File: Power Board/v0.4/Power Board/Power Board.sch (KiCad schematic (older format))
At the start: 26 parts, among them J1 Battery In, J2 JST B2PS-VH, J3 JST B2PS-VH, J4 JST B2PS-VH, J5 JST B2PS-VH, J6 JST B2PS-VH, J7 JST B2PS-VH, J8 Molex 70553-0006, SW1 SW_Push

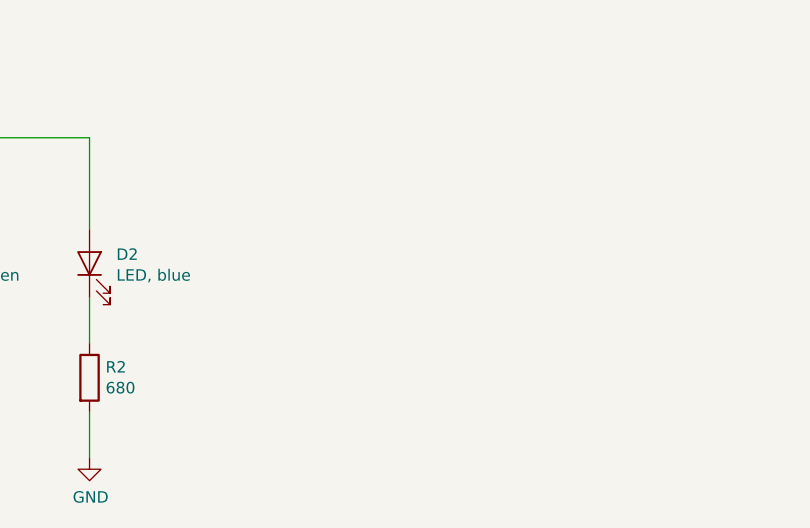
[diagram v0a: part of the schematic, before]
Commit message: Update panel power with Cin, Cout.
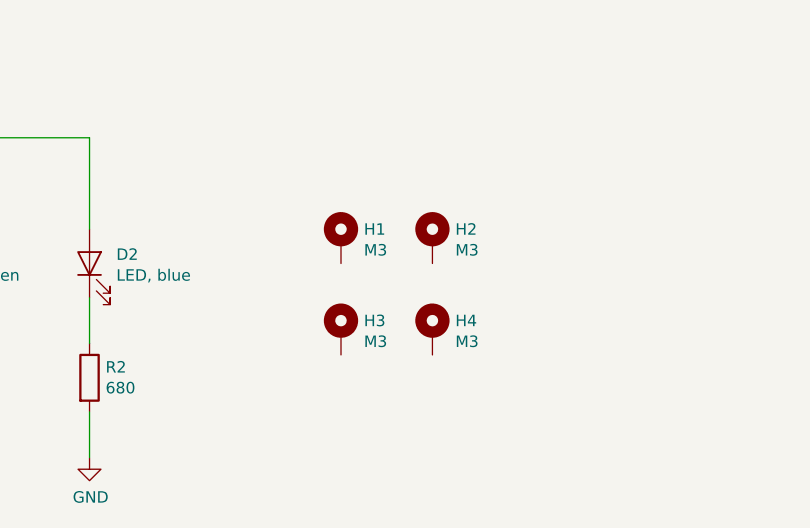
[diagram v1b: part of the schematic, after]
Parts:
- added H1, H2, H3, H4: M3, MountingHole:MountingHole_3.2mm_M3_Pad_Via, symbol Mechanical:MountingHole_Pad
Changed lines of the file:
@@
+	1    0    0    -1
+$EndComp
+$Comp
+L Mechanical:MountingHole_Pad H1
+U 1 1 5CADB5EA
+P 3900 6400
+F 0 "H1" H 4000 6449 50  0000 L CNN
+F 1 "M3" H 4000 6358 50  0000 L CNN
+F 2 "MountingHole:MountingHole_3.2mm_M3_Pad_Via" H 3900 6400 50  0001 C CNN
+F 3 "~" H 3900 6400 50  0001 C CNN
+F 4 "-" H 0   0   50  0001 C CNN "Digikey No."
+F 5 "-" H 0   0   50  0001 C CNN "Manufacturer"
+F 6 "-" H 0   0   50  0001 C CNN "Part No."
+	1    3900 6400
+	1    0    0    -1
+$EndComp
+$Comp
+L Mechanical:MountingHole_Pad H2
+U 1 1 5CADBAB3
+P 4300 6400
+F 0 "H2" H 4400 6449 50  0000 L CNN
+F 1 "M3" H 4400 6358 50  0000 L CNN
+F 2 "MountingHole:MountingHole_3.2mm_M3_Pad_Via" H 4300 6400 50  0001 C CNN
+F 3 "~" H 4300 6400 50  0001 C CNN
+F 4 "-" H 0   0   50  0001 C CNN "Digikey No."
+F 5 "-" H 0   0   50  0001 C CNN "Manufacturer"
+F 6 "-" H 0   0   50  0001 C CNN "Part No."
+	1    4300 6400
+	1    0    0    -1
+$EndComp
+$Comp
+L Mechanical:MountingHole_Pad H4
+U 1 1 5CADBCBF
+P 4300 6800
+F 0 "H4" H 4400 6849 50  0000 L CNN
+F 1 "M3" H 4400 6758 50  0000 L CNN
+F 2 "MountingHole:MountingHole_3.2mm_M3_Pad_Via" H 4300 6800 50  0001 C CNN
+F 3 "~" H 4300 6800 50  0001 C CNN
+F 4 "-" H 0   0   50  0001 C CNN "Digikey No."
+F 5 "-" H 0   0   50  0001 C CNN "Manufacturer"
+F 6 "-" H 0   0   50  0001 C CNN "Part No."
+	1    4300 6800
+	1    0    0    -1
+$EndComp
+$Comp
+L Mechanical:MountingHole_Pad H3
+U 1 1 5CADBD88
+P 3900 6800
+F 0 "H3" H 4000 6849 50  0000 L CNN
+F 1 "M3" H 4000 6758 50  0000 L CNN
+F 2 "MountingHole:MountingHole_3.2mm_M3_Pad_Via" H 3900 6800 50  0001 C CNN
+F 3 "~" H 3900 6800 50  0001 C CNN
+F 4 "-" H 0   0   50  0001 C CNN "Digikey No."
+F 5 "-" H 0   0   50  0001 C CNN "Manufacturer"
+F 6 "-" H 0   0   50  0001 C CNN "Part No."
+	1    3900 6800
 	1    0    0    -1
 $EndComp

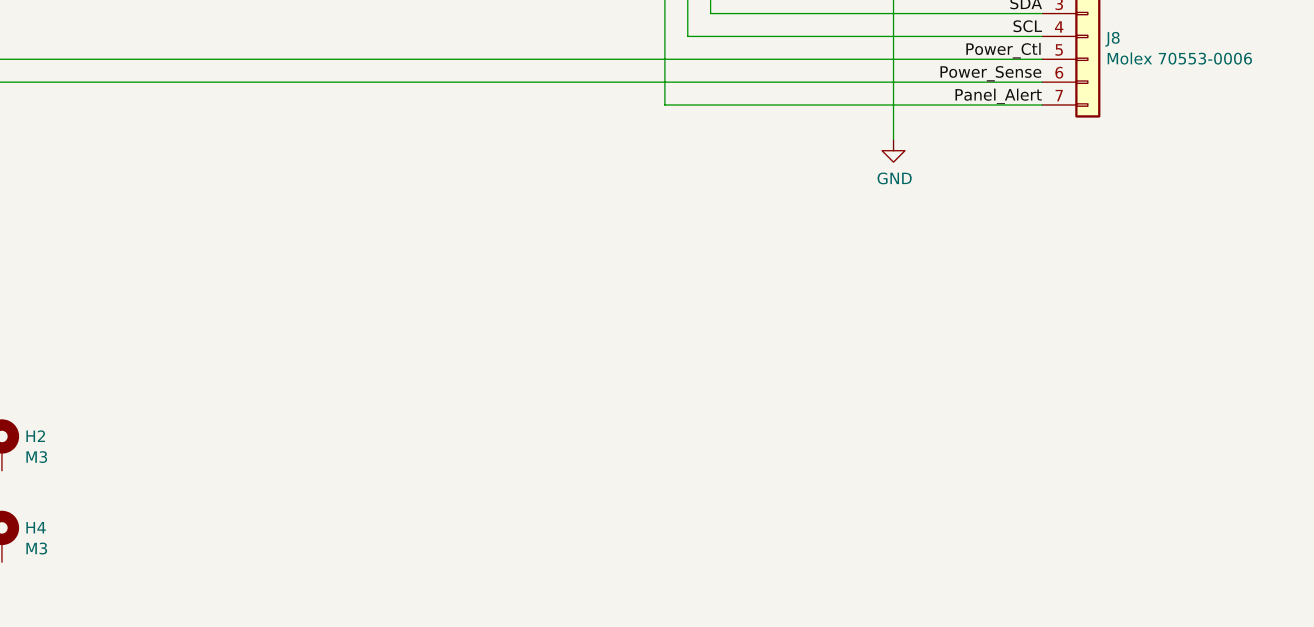
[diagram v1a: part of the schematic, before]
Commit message: Preliminary Layout Started
Have most of the components moved to reasonable locations.
Initial layout placeholders to get a general sense of connections.
Added a sheet with the MPU-9250 Circuit but not pushed to board yet.
Still need to add a lot of copper pours and stitching.
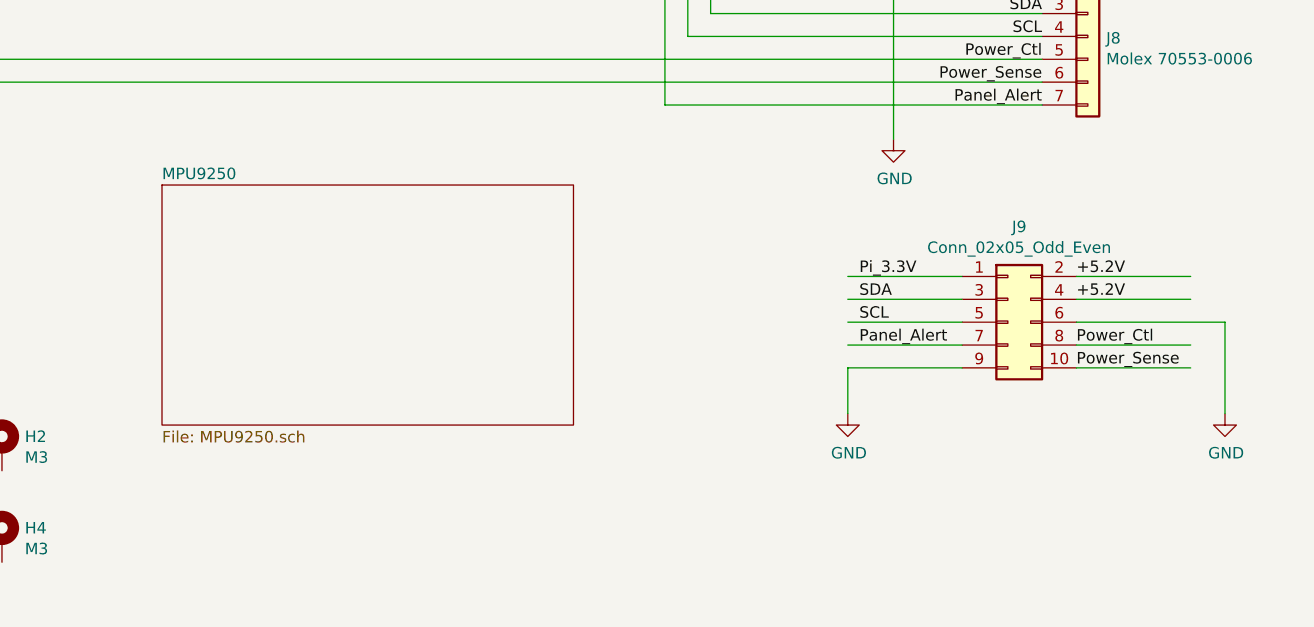
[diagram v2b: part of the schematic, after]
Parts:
- added J9: Conn_02x05_Odd_Even, Connector_PinHeader_2.54mm:PinHeader_2x05_P2.54mm_Vertical, symbol Connector_Generic:Conn_02x05_Odd_Even
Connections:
- net labels added: Pi_3.3V
- wire segments 75 -> 87
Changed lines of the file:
@@
 $Descr USLetter 11000 8500
 encoding utf-8
-Sheet 1 3
+Sheet 1 4
 Title "LED Cube Power Board"
 Date ""
@@
 	1    0    0    -1
 $EndComp
+$Comp
+L Connector_Generic:Conn_02x05_Odd_Even J9
+U 1 1 5CB857FA
+P 8700 5850
+F 0 "J9" H 8750 6267 50  0000 C CNN
+F 1 "Conn_02x05_Odd_Even" H 8750 6176 50  0000 C CNN
+F 2 "Connector_PinHeader_2.54mm:PinHeader_2x05_P2.54mm_Vertical" H 8700 5850 50  0001 C CNN
+F 3 "~" H 8700 5850 50  0001 C CNN
+	1    8700 5850
+	1    0    0    -1
+$EndComp
+$Sheet
+S 5000 5250 1800 1050
+U 5CBBBF0A
+F0 "MPU9250" 50
+F1 "MPU9250.sch" 50
+$EndSheet
+Text Label 9000 5650 0    50   ~ 0
++5.2V
+Text Label 9000 5750 0    50   ~ 0
++5.2V
+Text Label 8050 5650 0    50   ~ 0
+Pi_3.3V
+Text Label 8050 5750 0    50   ~ 0
+SDA
+Text Label 8050 5850 0    50   ~ 0
+SCL
+Text Label 8050 5950 0    50   ~ 0
+Panel_Alert
+Text Label 9000 5950 0    50   ~ 0
+Power_Ctl
+Text Label 9000 6050 0    50   ~ 0
+Power_Sense
+Wire Wire Line
+	9000 5650 9500 5650
+Wire Wire Line
+	9000 5750 9500 5750
+Wire Wire Line
+	9000 5950 9500 5950
+Wire Wire Line
+	9000 6050 9500 6050
+Wire Wire Line
+	9650 5850 9650 6250
+Wire Wire Line
+	9000 5850 9650 5850
+Wire Wire Line
+	8000 5650 8500 5650
+Wire Wire Line
+	8000 5750 8500 5750
+Wire Wire Line
+	8000 5850 8500 5850
+Wire Wire Line
+	8000 5950 8500 5950
+Wire Wire Line
+	8000 6050 8500 6050
+Wire Wire Line
+	8000 6050 8000 6250
+$Comp
+L power:GND #PWR?
+U 1 1 5CC03CFB
+P 8000 6250
+F 0 "#PWR?" H 8000 6000 50  0001 C CNN
+F 1 "GND" H 8005 6077 50  0000 C CNN
+F 2 "" H 8000 6250 50  0001 C CNN
+F 3 "" H 8000 6250 50  0001 C CNN
+	1    8000 6250
+	1    0    0    -1
+$EndComp
+$Comp
+L power:GND #PWR?
+U 1 1 5CC046D5
+P 9650 6250
+F 0 "#PWR?" H 9650 6000 50  0001 C CNN
+F 1 "GND" H 9655 6077 50  0000 C CNN
+F 2 "" H 9650 6250 50  0001 C CNN
+F 3 "" H 9650 6250 50  0001 C CNN
+	1    9650 6250
+	1    0    0    -1
+$EndComp

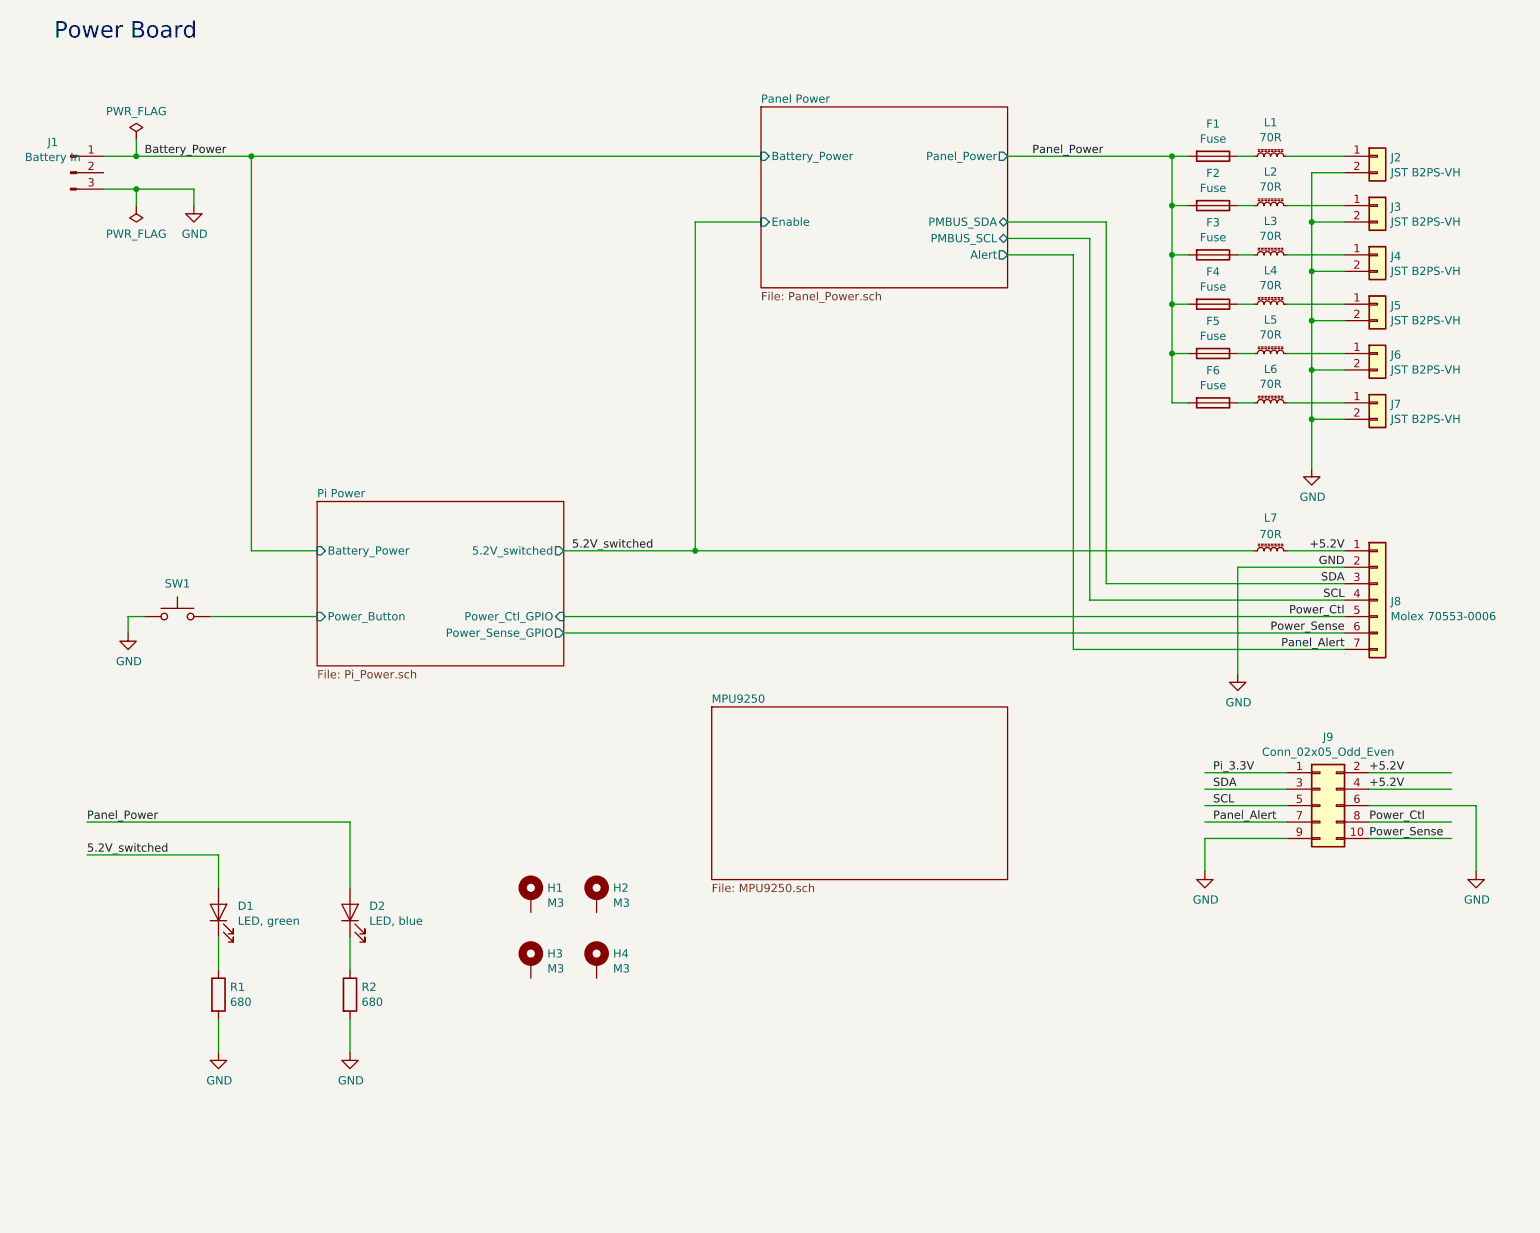
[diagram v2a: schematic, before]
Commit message: Widen board to 70mm, delineate mechanical keepout zones.
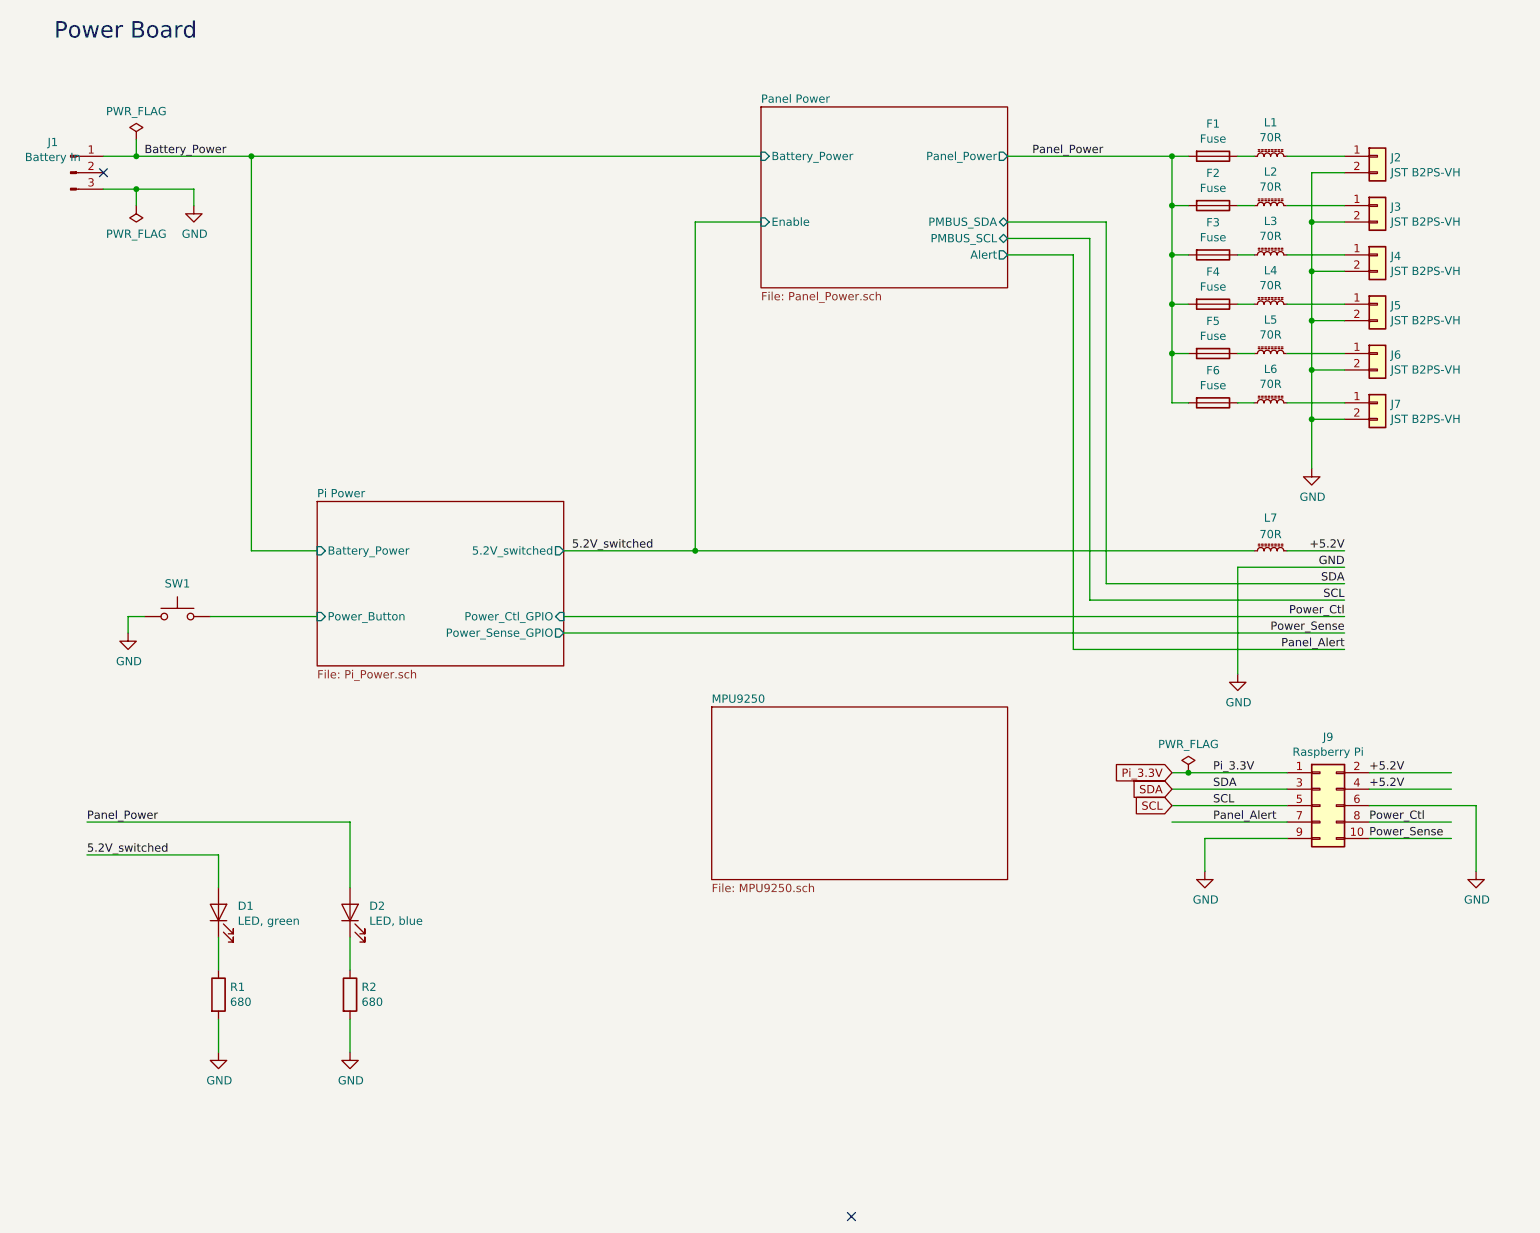
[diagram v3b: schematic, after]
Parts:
- removed H1, H2, H3, H4: M3, MountingHole:MountingHole_3.2mm_M3_Pad_Via, symbol Mechanical:MountingHole_Pad
- removed J8: Molex 70553-0006, Power_Board:Molex_SL_70553-0006, symbol Connector_Generic:Conn_01x07
- J9: value Conn_02x05_Odd_Even -> Raspberry Pi; footprint Connector_PinHeader_2.54mm:PinHeader_2x05_P2.54mm_Vertical -> Connector_JST:JST_PUD_S10B-PUDSS-1_2x05_P2.00mm_Horizontal
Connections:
- wire segments 87 -> 88
- no-connect marks 0 -> 2
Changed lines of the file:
@@
-$EndComp
-$Comp
-L Connector_Generic:Conn_01x07 J8
-U 1 1 5C997D7E
-P 9050 4600
-F 0 "J8" H 9130 4592 50  0000 L CNN
-F 1 "Molex 70553-0006" H 9130 4501 50  0000 L CNN
-F 2 "Power_Board:Molex_SL_70553-0006" H 9050 4600 50  0001 C CNN
-F 3 "~" H 9050 4600 50  0001 C CNN
-F 4 "WM4904-ND" H -750 350 50  0001 C CNN "Digikey No."
-F 5 "Molex" H -750 350 50  0001 C CNN "Manufacturer"
-F 6 "70553-0005" H -750 350 50  0001 C CNN "Part No."
-	1    9050 4600
-	1    0    0    -1
 $EndComp
 $Comp
@@
 $EndComp
 $Comp
-L Mechanical:MountingHole_Pad H1
-U 1 1 5CADB5EA
-P 3900 6400
-F 0 "H1" H 4000 6449 50  0000 L CNN
-F 1 "M3" H 4000 6358 50  0000 L CNN
-F 2 "MountingHole:MountingHole_3.2mm_M3_Pad_Via" H 3900 6400 50  0001 C CNN
-F 3 "~" H 3900 6400 50  0001 C CNN
-F 4 "-" H 0   0   50  0001 C CNN "Digikey No."
-F 5 "-" H 0   0   50  0001 C CNN "Manufacturer"
-F 6 "-" H 0   0   50  0001 C CNN "Part No."
-	1    3900 6400
-	1    0    0    -1
-$EndComp
-$Comp
-L Mechanical:MountingHole_Pad H2
-U 1 1 5CADBAB3
-P 4300 6400
-F 0 "H2" H 4400 6449 50  0000 L CNN
-F 1 "M3" H 4400 6358 50  0000 L CNN
-F 2 "MountingHole:MountingHole_3.2mm_M3_Pad_Via" H 4300 6400 50  0001 C CNN
-F 3 "~" H 4300 6400 50  0001 C CNN
-F 4 "-" H 0   0   50  0001 C CNN "Digikey No."
-F 5 "-" H 0   0   50  0001 C CNN "Manufacturer"
-F 6 "-" H 0   0   50  0001 C CNN "Part No."
-	1    4300 6400
-	1    0    0    -1
-$EndComp
-$Comp
-L Mechanical:MountingHole_Pad H4
-U 1 1 5CADBCBF
-P 4300 6800
-F 0 "H4" H 4400 6849 50  0000 L CNN
-F 1 "M3" H 4400 6758 50  0000 L CNN
-F 2 "MountingHole:MountingHole_3.2mm_M3_Pad_Via" H 4300 6800 50  0001 C CNN
-F 3 "~" H 4300 6800 50  0001 C CNN
-F 4 "-" H 0   0   50  0001 C CNN "Digikey No."
-F 5 "-" H 0   0   50  0001 C CNN "Manufacturer"
-F 6 "-" H 0   0   50  0001 C CNN "Part No."
-	1    4300 6800
-	1    0    0    -1
-$EndComp
-$Comp
-L Mechanical:MountingHole_Pad H3
-U 1 1 5CADBD88
-P 3900 6800
-F 0 "H3" H 4000 6849 50  0000 L CNN
-F 1 "M3" H 4000 6758 50  0000 L CNN
-F 2 "MountingHole:MountingHole_3.2mm_M3_Pad_Via" H 3900 6800 50  0001 C CNN
-F 3 "~" H 3900 6800 50  0001 C CNN
-F 4 "-" H 0   0   50  0001 C CNN "Digikey No."
-F 5 "-" H 0   0   50  0001 C CNN "Manufacturer"
-F 6 "-" H 0   0   50  0001 C CNN "Part No."
-	1    3900 6800
-	1    0    0    -1
-$EndComp
-$Comp
 L Connector_Generic:Conn_02x05_Odd_Even J9
 U 1 1 5CB857FA
 P 8700 5850
 F 0 "J9" H 8750 6267 50  0000 C CNN
-F 1 "Conn_02x05_Odd_Even" H 8750 6176 50  0000 C CNN
-F 2 "Connector_PinHeader_2.54mm:PinHeader_2x05_P2.54mm_Vertical" H 8700 5850 50  0001 C CNN
+F 1 "Raspberry Pi" H 8750 6176 50  0000 C CNN
+F 2 "Connector_JST:JST_PUD_S10B-PUDSS-1_2x05_P2.00mm_Horizontal" H 8700 5850 50  0001 C CNN
 F 3 "~" H 8700 5850 50  0001 C CNN
 	1    8700 5850
@@
 	9000 5850 9650 5850
 Wire Wire Line
-	8000 5650 8500 5650
+	7800 5650 7900 5650
 Wire Wire Line
-	8000 5750 8500 5750
+	7800 5750 8500 5750
 Wire Wire Line
-	8000 5850 8500 5850
+	7800 5850 8500 5850
 Wire Wire Line
-	8000 5950 8500 5950
+	7800 5950 8500 5950
 Wire Wire Line
 	8000 6050 8500 6050
@@
 	8000 6050 8000 6250
 $Comp
-L power:GND #PWR?
+L power:GND #PWR0109
 U 1 1 5CC03CFB
 P 8000 6250
-F 0 "#PWR?" H 8000 6000 50  0001 C CNN
+F 0 "#PWR0109" H 8000 6000 50  0001 C CNN
 F 1 "GND" H 8005 6077 50  0000 C CNN
 F 2 "" H 8000 6250 50  0001 C CNN
@@
 $EndComp
 $Comp
-L power:GND #PWR?
+L power:GND #PWR0110
 U 1 1 5CC046D5
 P 9650 6250
-F 0 "#PWR?" H 9650 6000 50  0001 C CNN
+F 0 "#PWR0110" H 9650 6000 50  0001 C CNN
 F 1 "GND" H 9655 6077 50  0000 C CNN
 F 2 "" H 9650 6250 50  0001 C CNN
@@
 	1    0    0    -1
 $EndComp
+NoConn ~ 1300 2000
+NoConn ~ 5850 8350
+Text GLabel 7800 5650 0    50   Input ~ 0
+Pi_3.3V
+Text GLabel 7800 5750 0    50   Input ~ 0
+SDA
+Text GLabel 7800 5850 0    50   Input ~ 0
+SCL
+$Comp
+L power:PWR_FLAG #FLG0101
+U 1 1 5CB60B57
+P 7900 5650
+F 0 "#FLG0101" H 7900 5725 50  0001 C CNN
+F 1 "PWR_FLAG" H 7900 5823 50  0000 C CNN
+F 2 "" H 7900 5650 50  0001 C CNN
+F 3 "~" H 7900 5650 50  0001 C CNN
+	1    7900 5650
+	1    0    0    -1
+$EndComp
+Connection ~ 7900 5650
+Wire Wire Line
+	7900 5650 8500 5650
 $EndSCHEMATC
